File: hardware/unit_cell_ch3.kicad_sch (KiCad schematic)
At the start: 5 parts, among them J3 Conn_RTD_4W

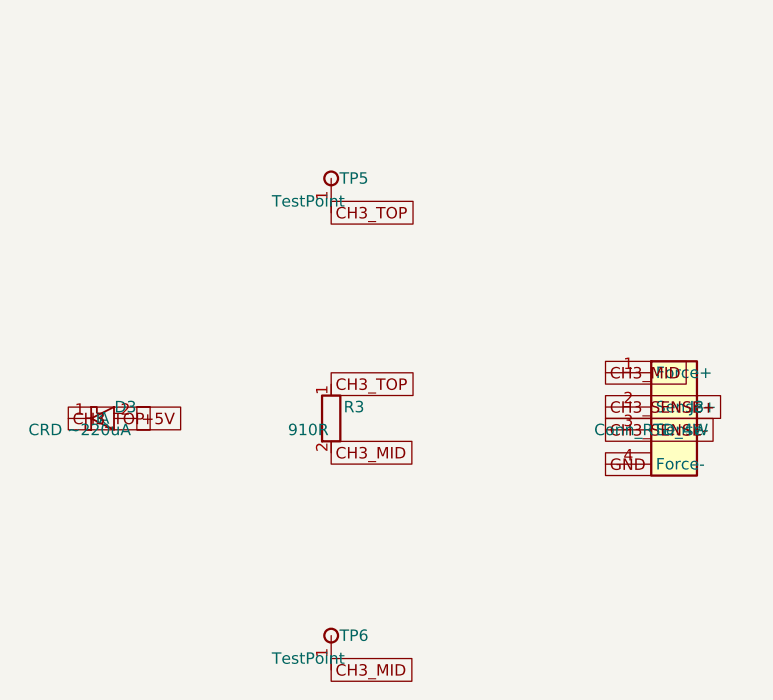
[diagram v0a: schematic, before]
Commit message: trackE: wire-up pass -- drawn wires + power symbols (netlist unchanged)
Convert the label-based capture to a conventionally drawn schematic: unit cells
as a drawn series current-loop (+5V/GND power symbols, CRD->R_ref->RTD, tapped
TOP/MID to TPs+labels); acquisition/power_io pins stub to power symbols/labels;
cross-sheet signals stay labelled. Fixed a y-down rotation bug (CRD anode/cathode
swap) by rotating the CRD 90 not 270.

ERC 0 errors / 0 warnings. Netlist node-for-node IDENTICAL to the pre-wiring
verified netlist (21 nets, diff empty); sim/netlists refreshed.

Co-Authored-By: Claude Opus 4.8 <noreply@anthropic.com>
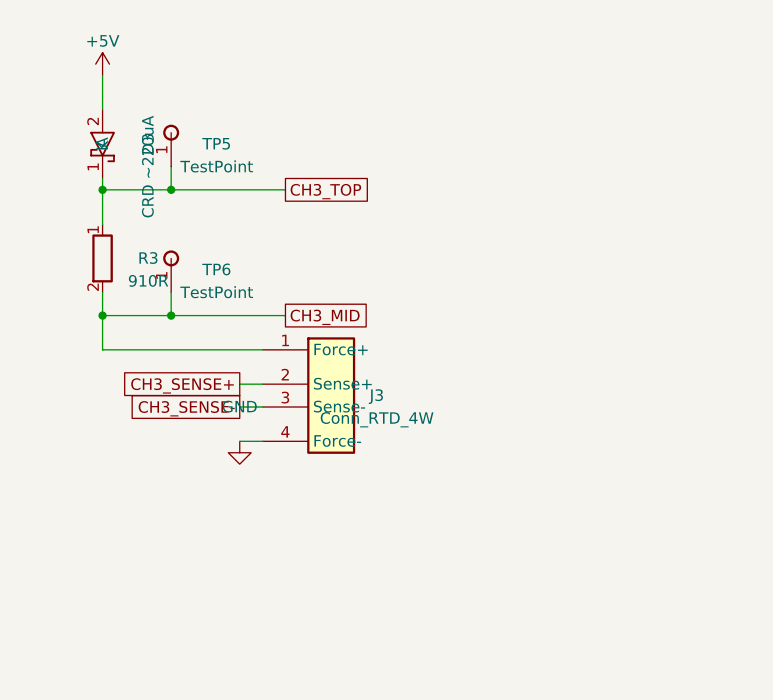
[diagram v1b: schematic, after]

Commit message: rev-B: real Digi-Key parts + layout review (copper unchanged)
Independent layout review + adversarial verify: 4-layer split planes, single-
point analog/digital GND tie, Kelvin intact -> fabricable (yes-with-fixes).
Real Digi-Key MPNs on the whole BOM; fixed RTD conn P/N (1729160 6-pos ->
1729144 4-pos) and R_ref tempco (25ppm -> Vishay TNPU1206 <=10ppm per spec).
ERC 0/0, DRC 0/0. Open decision: sense-line RC filter (see USER_MANUAL 8.5).

Co-Authored-By: Claude Opus 4.8 <noreply@anthropic.com>
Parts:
- J3: MPN 1729160 (MKDS 1,5/4-5,08) -> 1729144 (MKDS 1,5/4-5,08)
- R3: MPN RG3216P-911-B-T5 -> TNPU1206 910R 0.1% 10ppm (confirm code); Manufacturer Susumu (representative; any <=10 ppm/C thin-film ~910R is a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 -> Vishay (>=10ppm/C thin-film; see BOM_REVIEW)
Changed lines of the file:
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@@
 			)
 		)
-		(property "MPN" "RG3216P-911-B-T5"
+		(property "MPN" "TNPU1206 910R 0.1% 10ppm (confirm code)"
 			(at 50.8 45.72 0)
 			(show_name no)
@@
 			)
 		)
-		(property "Manufacturer" "Susumu (representative; any <=10 ppm/C thin-film ~910R is acceptable)"
+		(property "Manufacturer" "Vishay (>=10ppm/C thin-film; see BOM_REVIEW)"
 			(at 50.8 45.72 0)
 			(show_name no)
@@
 			)
 		)
-		(property "MPN" "1729160 (MKDS 1,5/4-5,08)"
+		(property "MPN" "1729144 (MKDS 1,5/4-5,08)"
 			(at 76.2 60.96 0)
 			(show_name no)

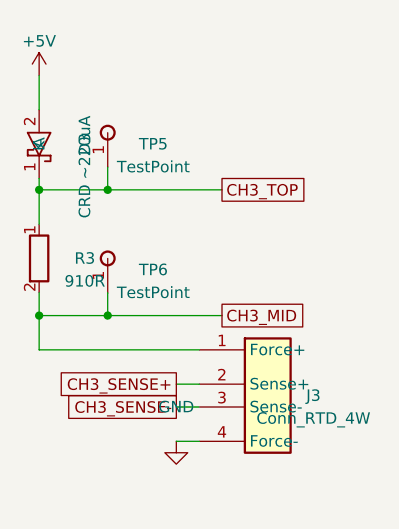
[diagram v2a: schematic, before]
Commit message: schematic: restructure for auditability (page1 = ch1+acquisition+power, drawn wires)
Page 1 merges unit_cell_ch1 + acquisition + power_io with 28 drawn join wires
(CH1 taps -> U1 AIN0/1, Kelvin sense pairs -> J4, I2C bus U1->U2->J5); pages
2-3 = CH2/CH3 cells. Blocks rigidly translated, labels kept: netlist verified
node-for-node IDENTICAL (21 nets, 80 nodes) vs pre-restructure; ERC 0/0; DRC
parity unchanged (47 cosmetic). Verified by 5-agent workflow (independent
netlist oracle, gates, visual audit, BOM byte-identical, adversarial trace);
visual-audit findings fixed (label flips reverted, power-text normalized,
values repositioned, J4 pin names hidden, pages 2-3 title blocks). PCB
untouched (binds by refdes).

Co-Authored-By: Claude Opus 4.8 <noreply@anthropic.com>
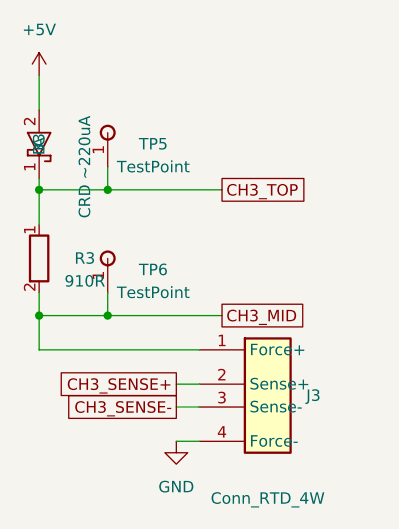
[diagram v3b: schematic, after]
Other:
- title: (none) -> RTD Readout - unit cell CH3
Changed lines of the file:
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@@
 	(generator_version "10.0")
 	(paper "A3")
+	(title_block
+		(title "RTD Readout - unit cell CH3")
+		(rev "B")
+	)
 	(symbol
 		(lib_id "rtd-readout:CRD_1N5283")
@@
 		(dnp no)
 		(property "Reference" "D3"
-			(at 55.88 33.02 0)
+			(at 50.8 33.02 0)
 			(show_name no)
 			(do_not_autoplace no)
@@
 		)
 		(property "Value" "Conn_RTD_4W"
-			(at 81.28 63.5 0)
+			(at 76.2 72.39 0)
 			(show_name no)
 			(do_not_autoplace no)
@@
 		(dnp no)
 		(property "Reference" "#PWR005" (at 50.8 19.05 0) (effects (font (size 1.27 1.27)) (hide yes)))
-		(property "Value" "+5V" (at 50.8 21.59 0) (effects (font (size 1.27 1.27))))
+		(property "Value" "+5V" (at 50.8 20.32 0) (effects (font (size 1.27 1.27))))
 		(pin "1")
 		(instances (project "rtd-readout" (path "/6ce05a31-b5af-4e3a-a08f-83802c091454/7f1cb510-1a57-40b5-ab4c-4fc79046c09e" (reference "#PWR005") (unit 1))))
@@
 		(dnp no)
 		(property "Reference" "#PWR006" (at 66.04 59.69 0) (effects (font (size 1.27 1.27)) (hide yes)))
-		(property "Value" "GND" (at 66.04 62.23 0) (effects (font (size 1.27 1.27))))
+		(property "Value" "GND" (at 66.04 71.12 0) (effects (font (size 1.27 1.27))))
 		(pin "1")
 		(instances (project "rtd-readout" (path "/6ce05a31-b5af-4e3a-a08f-83802c091454/7f1cb510-1a57-40b5-ab4c-4fc79046c09e" (reference "#PWR006") (unit 1))))

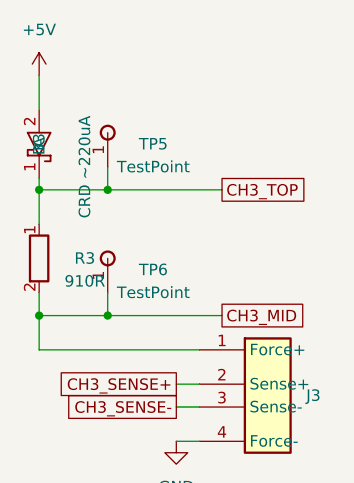
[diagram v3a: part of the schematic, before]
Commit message: rev-E: DFM/availability respin - CRD J500 TO-92, 0805 caps, R_ref 820R
Hand-assembly + live-Digi-Key-verified changes (all adversarially fact-checked):
- D1-D4: CDLL5283 MELF (unbuyable, 0 stock/40wk MOQ) -> LIS J500 TO-92 2L;
  new mirrored footprint TO-92-2_CRD-J500 (pad1=K at flat-to-silk insertion,
  0.8mm drill), 8 F.Cu stubs bridge old MELF trace ends to the THT pads.
- C1-C8: 0603 -> 0805 (Samsung CL21B104KBCNNNC / CL21A106KACLRNC; old Murata
  parts obsolete/backordered). C5-C8 keep the back-side across-J4 scheme.
- R_ref: 910R -> 820R (KOA RN73H2BTTD8200B10, 0.1%, 10ppm/C) - J500 band is
  +/-20%, 910R would clip the ADS1115 +/-0.256V range at band max.
- SPICE harness re-pointed (240uA, 820R, VL 1.2V, Z 4Meg; test4 gate <95% FS
  at kc=1.2); docs/spec/BOM_REVIEW/host defaults updated.

Gates: ERC 0/0, DRC 0 violations / 0 unconnected, SPICE 7/7 PASS
(t4: V_ref at band max = 237 mV = 93% FS, 14.9 bits).

Co-Authored-By: Claude Fable 5 <noreply@anthropic.com>
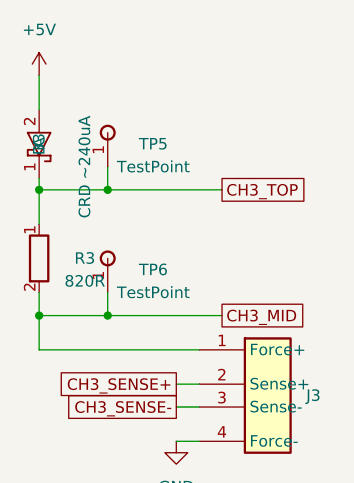
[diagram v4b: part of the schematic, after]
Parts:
- D3: value CRD ~220uA -> CRD ~240uA; footprint rtd-readout:D_MELF -> rtd-readout:TO-92-2_CRD-J500; Current_nom ~0.22 mA (1N5283), +/-10%; stability over one scan is what 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 -> ~0.24 mA (J500), +/-20% band (0.192-0.288 mA); stability ov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; MPN CDLL5283 -> J500 TO-92 2L; Manufacturer Microchip (Microsemi / ex-Central Semiconductor) -> Linear Integrated Systems; Polarity Pin 1 = K (cathode, banded end). Pin 2 = A (anode). Matches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 -> Pin 1 = K (cathode). Pin 2 = A (anode). J500 TO-92 physical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
- R3: value 910R -> 820R; MPN TNPU1206 910R 0.1% 10ppm (confirm code) -> RN73H2BTTD8200B10
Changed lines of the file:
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@@
 			)
 		)
-		(property "Value" "CRD ~220uA"
+		(property "Value" "CRD ~240uA"
 			(at 55.88 35.56 0)
 			(show_name no)
@@
 			)
 		)
-		(property "Footprint" "rtd-readout:D_MELF"
+		(property "Footprint" "rtd-readout:TO-92-2_CRD-J500"
 			(at 50.8 33.02 0)
 			(show_name no)
@@
 			)
 		)
-		(property "Datasheet" "https://www.microchip.com/en-us/product/cdll5283-current-regulator-diode"
+		(property "Datasheet" "https://www.linearsystems.com/currentregulatingdiodes/j500-series"
 			(at 50.8 33.02 0)
 			(show_name no)
@@
 			)
 		)
-		(property "Description" "Current-regulator diode (constant-current diode), ~0.22 mA, two-terminal, DO-213AB MELF. Sets the per-channel excitation current; exact value is measured live and cancels (board_spec.md). Anode -> +V rail, cathode -> R_ref."
+		(property "Description" "Current-regulator diode (constant-current diode), ~0.24 mA (LIS J500, 0.192-0.288 mA band), two-terminal, TO-92 2-lead THT. Sets the per-channel excitation current; exact value is measured live and cancels (board_spec.md). Anode -> +V rail, cathode -> R_ref."
 			(at 50.8 33.02 0)
 			(show_name no)
@@
 			)
 		)
-		(property "MPN" "CDLL5283"
+		(property "MPN" "J500 TO-92 2L"
 			(at 50.8 33.02 0)
 			(show_name no)
@@
 			)
 		)
-		(property "Manufacturer" "Microchip (Microsemi / ex-Central Semiconductor)"
+		(property "Manufacturer" "Linear Integrated Systems"
 			(at 50.8 33.02 0)
 			(show_name no)
@@
 			)
 		)
-		(property "Polarity" "Pin 1 = K (cathode, banded end). Pin 2 = A (anode). Matches D_MELF pad 1 = cathode."
+		(property "Polarity" "Pin 1 = K (cathode). Pin 2 = A (anode). J500 TO-92 physical: facing the flat/marked face, left lead = A, right lead = K; the TO-92-2_CRD-J500 footprint silk is mirrored so matching the flat face to the silk outline puts K in pad 1."
 			(at 50.8 33.02 0)
 			(show_name no)
@@
 			)
 		)
-		(property "Current_nom" "~0.22 mA (1N5283), +/-10%; stability over one scan is what matters, not absolute value."
+		(property "Current_nom" "~0.24 mA (J500), +/-20% band (0.192-0.288 mA); stability over one scan is what matters, not absolute value."
 			(at 50.8 33.02 0)
 			(show_name no)
@@
 			)
 		)
-		(property "ki_keywords" "CRD current regulator diode constant current 1N5283 CDLL5283 RTD excitation MELF"
+		(property "ki_keywords" "CRD current regulator diode constant current J500 RTD excitation TO-92"
 			(at 50.8 33.02 0)
 			(show_name no)
@@
 			)
 		)
-		(property "ki_fp_filters" "D*MELF*"
+		(property "ki_fp_filters" "TO?92*"
 			(at 50.8 33.02 0)
 			(show_name no)
@@
 			)
 		)
-		(property "Value" "910R"
+		(property "Value" "820R"
 			(at 55.88 48.26 0)
 			(show_name no)
@@
 			)
 		)
-		(property "Datasheet" "https://www.susumu.co.jp/common/pdf/n_catalog_partition06_en.pdf"
+		(property "Datasheet" "https://www.koaspeer.com/pdfs/RN73H.pdf"
 			(at 50.8 45.72 0)
 			(show_name no)
@@
 			)
 		)
-		(property "Description" "Reference resistor for ratiometric current sense. ~910 ohm sets V_ref ~200 mV nominal inside the ADS1115 +/-0.256 V range. BINDING SPEC = tempco/stability, NOT absolute value (cross-cal constant C absorbs the value; board_spec.md s.R_ref)."
+		(property "Description" "Reference resistor for ratiometric current sense. 820 ohm sets V_ref ~197 mV nominal, <=236 mV at the J500 guaranteed-max 0.288 mA, inside the ADS1115 +/-0.256 V range. BINDING SPEC = tempco/stability, NOT absolute value (cross-cal constant C absorbs the value; board_spec.md s.R_ref)."
 			(at 50.8 45.72 0)
 			(show_name no)
@@
 			)
 		)
-		(property "MPN" "TNPU1206 910R 0.1% 10ppm (confirm code)"
+		(property "MPN" "RN73H2BTTD8200B10"
 			(at 50.8 45.72 0)
 			(show_name no)

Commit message: rev-F: cryostat/stability respin - 100uA S-101T CRD, C0G sense path, 2ppm R_ref
Sensors are in a vacuum cryostat down to ~100 K; excitation lowered to cut
self-heating ~6x (0.3-1.6 uW nominal), measurement path upgraded to
precision-grade passives. All parts live-verified on Digi-Key with
adversarial fact-checks:
- D1-D4: LIS J500 TO-92 -> SEMITEC S-101T (100uA typ, band 0.05-0.21mA,
  SMD flat 2-lead); custom footprint from SEMITEC's recommended land
  pattern (1.2x1.6mm pads, 3.4mm centers, cathode-band marking).
- R_ref: 820R 10ppm -> 1.00k +/-0.05% +/-2ppm/C (Vishay TNPU12061K00AWEN00);
  V_ref 100mV nom, 210mV = 82% FS at band max. Reference is no longer the
  drift limiter (by design).
- C5-C8: X7R 0805 -> C0G/NP0 0.1uF 50V 1206 (Murata GRM31C5C1H104JA01L);
  moved east of J4 on B.Cu with routed stubs (1206 body cannot straddle
  the pin holes). R7-R14: 1% thick film -> 0.1% 25ppm thin film (Susumu).
- Sims: 100uA/1k/2ppm/VL 2.0/RTD window extended to 100 K (Pt100 29.5R);
  band sweeps 0.5-2.1x; t3 criterion re-gated to 'R_ref not limiting';
  t6 noise assumption made per-read (4-conversion average).

Gates: ERC 0/0, DRC 0 violations / 0 unconnected, SPICE 7/7 PASS.

Co-Authored-By: Claude Fable 5 <noreply@anthropic.com>
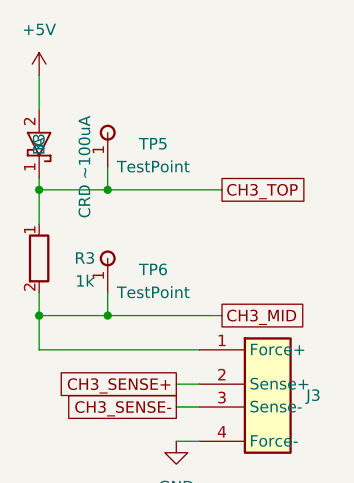
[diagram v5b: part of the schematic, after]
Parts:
- D3: value CRD ~240uA -> CRD ~100uA; footprint rtd-readout:TO-92-2_CRD-J500 -> rtd-readout:D_SEMITEC_S-101T; Current_nom ~0.24 mA (J500), +/-20% band (0.192-0.288 mA); stability ov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 -> ~0.10 mA typ (S-101T), band 0.05-0.21 mA (-50%/+110%); stab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; MPN J500 TO-92 2L -> S-101T; Manufacturer Linear Integrated Systems -> SEMITEC; Polarity Pin 1 = K (cathode). Pin 2 = A (anode). J500 TO-92 physical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 -> Pin 1 = K (cathode). Pin 2 = A (anode). S-101T physical: th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
- R3: value 820R -> 1k; MPN RN73H2BTTD8200B10 -> TNPU12061K00AWEN00
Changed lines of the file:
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@@
 			)
 		)
-		(property "Value" "CRD ~240uA"
+		(property "Value" "CRD ~100uA"
 			(at 55.88 35.56 0)
 			(show_name no)
@@
 			)
 		)
-		(property "Footprint" "rtd-readout:TO-92-2_CRD-J500"
+		(property "Footprint" "rtd-readout:D_SEMITEC_S-101T"
 			(at 50.8 33.02 0)
 			(show_name no)
@@
 			)
 		)
-		(property "Datasheet" "https://www.linearsystems.com/currentregulatingdiodes/j500-series"
+		(property "Datasheet" "https://www.semitec-global.com/uploads/2022/01/P22-23-CRD.pdf"
 			(at 50.8 33.02 0)
 			(show_name no)
@@
 			)
 		)
-		(property "Description" "Current-regulator diode (constant-current diode), ~0.24 mA (LIS J500, 0.192-0.288 mA band), two-terminal, TO-92 2-lead THT. Sets the per-channel excitation current; exact value is measured live and cancels (board_spec.md). Anode -> +V rail, cathode -> R_ref."
+		(property "Description" "Current-regulator diode (constant-current diode), ~0.10 mA (SEMITEC S-101T, 0.05-0.21 mA band), two-terminal, SMD flat 2-lead. rev-F: current lowered ~2.4x to cut RTD self-heating in the vacuum cryostat (sensors to ~100 K). Exact value is measured live and cancels (board_spec.md). Anode -> +V rail, cathode -> R_ref."
 			(at 50.8 33.02 0)
 			(show_name no)
@@
 			)
 		)
-		(property "MPN" "J500 TO-92 2L"
+		(property "MPN" "S-101T"
 			(at 50.8 33.02 0)
 			(show_name no)
@@
 			)
 		)
-		(property "Manufacturer" "Linear Integrated Systems"
+		(property "Manufacturer" "SEMITEC"
 			(at 50.8 33.02 0)
 			(show_name no)
@@
 			)
 		)
-		(property "Polarity" "Pin 1 = K (cathode). Pin 2 = A (anode). J500 TO-92 physical: facing the flat/marked face, left lead = A, right lead = K; the TO-92-2_CRD-J500 footprint silk is mirrored so matching the flat face to the silk outline puts K in pad 1."
+		(property "Polarity" "Pin 1 = K (cathode). Pin 2 = A (anode). S-101T physical: the CATHODE end carries a hatched band on the marked (top) face; place that band toward pad 1 (the silk bar + K marker side)."
 			(at 50.8 33.02 0)
 			(show_name no)
@@
 			)
 		)
-		(property "Current_nom" "~0.24 mA (J500), +/-20% band (0.192-0.288 mA); stability over one scan is what matters, not absolute value."
+		(property "Current_nom" "~0.10 mA typ (S-101T), band 0.05-0.21 mA (-50%/+110%); stability over one scan is what matters, not absolute value (huge spread and up to +2.1%/C Ip tempco are cancelled by the ratiometric readout)."
 			(at 50.8 33.02 0)
 			(show_name no)
@@
 			)
 		)
-		(property "ki_keywords" "CRD current regulator diode constant current J500 RTD excitation TO-92"
+		(property "ki_keywords" "CRD current regulator diode constant current SEMITEC S-101T RTD excitation SMD"
 			(at 50.8 33.02 0)
 			(show_name no)
@@
 			)
 		)
-		(property "ki_fp_filters" "TO?92*"
+		(property "ki_fp_filters" "D_SEMITEC*"
 			(at 50.8 33.02 0)
 			(show_name no)
@@
 			)
 		)
-		(property "Value" "820R"
+		(property "Value" "1k"
 			(at 55.88 48.26 0)
 			(show_name no)
@@
 			)
 		)
-		(property "Datasheet" "https://www.koaspeer.com/pdfs/RN73H.pdf"
+		(property "Datasheet" "https://www.vishay.com/docs/28779/tnpue3.pdf"
 			(at 50.8 45.72 0)
 			(show_name no)
@@
 			)
 		)
-		(property "Description" "Reference resistor for ratiometric current sense. 820 ohm sets V_ref ~197 mV nominal, <=236 mV at the J500 guaranteed-max 0.288 mA, inside the ADS1115 +/-0.256 V range. BINDING SPEC = tempco/stability, NOT absolute value (cross-cal constant C absorbs the value; board_spec.md s.R_ref)."
+		(property "Description" "Reference resistor for ratiometric current sense. 1.00 kohm sets V_ref ~100 mV nominal, <=210 mV at the S-101T band max 0.21 mA, inside the ADS1115 +/-0.256 V range. rev-F part is +/-2 ppm/C so R_ref is no longer the drift limiter. BINDING SPEC = tempco/stability, NOT absolute value (cross-cal absorbs the value; board_spec.md s.R_ref)."
 			(at 50.8 45.72 0)
 			(show_name no)
@@
 			)
 		)
-		(property "MPN" "RN73H2BTTD8200B10"
+		(property "MPN" "TNPU12061K00AWEN00"
 			(at 50.8 45.72 0)
 			(show_name no)

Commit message: rev-G: enclosure integration - 100x159.5 board, Hammond 1455N, RJ45/PT/KK I/O
Board resized to slide into a Hammond 1455N1601 extrusion (machinable end
panels, connectors proud/flush through cutouts). All parts live-verified
with adversarial fact-checks:
- RTD inputs: 4x Phoenix PT 1,5/5-3,5-H push-in blocks (pin 5 = cable
  shield to AGND); kept terminal blocks over RJ45 for bare cryo cables.
- T7 analog: Amphenol RJHSE-5380 shielded RA RJ45, T568 pair mapping
  (CH1=1/2, CH2=3/6, CH3=4/5, CH4=7/8), shield+chassis bond at the jack.
- T7 I2C: Molex KK 254 friction-lock header; pin numbers reversed (1<->4,
  2<->3) to make the fan planar - pigtail map in PANELS_AND_PINOUTS.md.
- Routing: via-free corridor (y 63-81) carries the 4 sense pairs to a C0G
  cap ladder + gated T568 fan; I2C as parallel diagonals; +5V south edge.
- Deliverables: docs/PANELS_AND_PINOUTS.md, panel machining DXFs, renders.

Gates: ERC 0/0, DRC 0 violations / 0 unconnected, SPICE 7/7 PASS.
DRC iteration trail: 92 -> 32 -> 8 -> 1 -> 0.

Co-Authored-By: Claude Fable 5 <noreply@anthropic.com>
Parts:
- J3: footprint rtd-readout:TerminalBlock_Phoenix_MKDS-1,5-4-5.08_1x04_P5.08mm_Horizontal -> rtd-readout:TerminalBlock_Phoenix_PT-1,5-5-3.5-H_1x05_P3.50mm_Horizontal; MPN 1729144 (MKDS 1,5/4-5,08) -> 1984646 (PT 1,5/5-3,5-H); Manufacturer Phoenix Contact (or any 4-pos 5.08 mm screw terminal) -> Phoenix Contact (PT 1,5/5-3,5-H, 3.5 mm pitch; pin 5 = cabl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
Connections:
- net GND: now also J3.5 (Shield)
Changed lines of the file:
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@@
 			)
 		)
-		(property "Footprint" "rtd-readout:TerminalBlock_Phoenix_MKDS-1,5-4-5.08_1x04_P5.08mm_Horizontal"
+		(property "Footprint" "rtd-readout:TerminalBlock_Phoenix_PT-1,5-5-3.5-H_1x05_P3.50mm_Horizontal"
 			(at 76.2 60.96 0)
 			(show_name no)
@@
 			)
 		)
-		(property "MPN" "1729144 (MKDS 1,5/4-5,08)"
-			(at 76.2 60.96 0)
-			(show_name no)
-			(do_not_autoplace no)
-			(hide yes)
-			(effects
-				(font
-					(size 1.27 1.27)
-				)
-			)
-		)
-		(property "Manufacturer" "Phoenix Contact (or any 4-pos 5.08 mm screw terminal)"
+		(property "MPN" "1984646 (PT 1,5/5-3,5-H)"
+			(at 76.2 60.96 0)
+			(show_name no)
+			(do_not_autoplace no)
+			(hide yes)
+			(effects
+				(font
+					(size 1.27 1.27)
+				)
+			)
+		)
+		(property "Manufacturer" "Phoenix Contact (PT 1,5/5-3,5-H, 3.5 mm pitch; pin 5 = cable shield to AGND)"
 			(at 76.2 60.96 0)
 			(show_name no)
@@
 		(pin "3")
 		(pin "4")
+		(pin "5")
 		(instances (project "rtd-readout" (path "/6ce05a31-b5af-4e3a-a08f-83802c091454/7f1cb510-1a57-40b5-ab4c-4fc79046c09e" (reference "J3") (unit 1))))
 	)
@@
 		(instances (project "rtd-readout" (path "/6ce05a31-b5af-4e3a-a08f-83802c091454/7f1cb510-1a57-40b5-ab4c-4fc79046c09e" (reference "#PWR006") (unit 1))))
 	)
+	(global_label "GND"
+		(shape input)
+		(at 68.58 68.58 180)
+		(effects
+			(font
+				(size 1.27 1.27)
+			)
+			(justify right)
+		)
+	)
 	(sheet_instances
